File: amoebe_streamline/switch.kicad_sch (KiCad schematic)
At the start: 2 parts

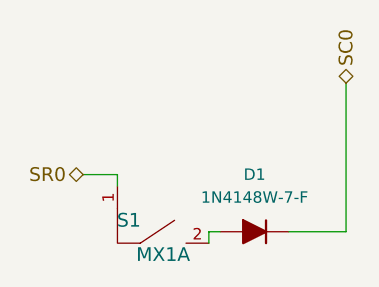
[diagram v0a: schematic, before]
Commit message: Finished schematic and routed traces
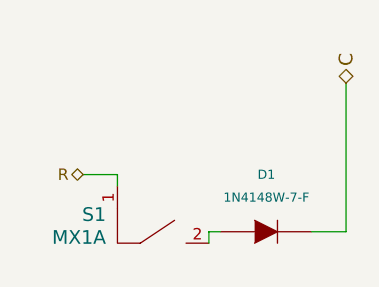
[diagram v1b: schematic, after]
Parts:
- removed D1: 1N4148W-7-F, Diode_SMD_AKL:D_SOD-123, symbol PCM_Diode_AKL:1N4148W
- removed S1: MX1A, amoeba-modules:Kailh_MX_Socket, symbol amoeba-king-rescue:MX1A-amoeba-rescue-amoeba-royale-rescue
- added D1: 1N4148W-7-F, Diode_SMD:D_SOD-123, symbol Amoebe_streamline:DIODE-amoeba-rescue
- added S1: MX1A, CustomFootprints:Kailh_socket_MX_reversible_platemount, symbol Amoebe_streamline:MX1A-amoeba-rescue
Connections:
- new net: D1.1 (A), S1.2
- new net C: D1.2 (K)
- new net R: S1.1
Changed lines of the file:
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@@
+    (stroke (width 0) (type default))
+  )
+  (wire (pts (xy 142.24 93.98) (xy 146.05 93.98))
     (stroke (width 0) (type default))
   )
   (wire (pts (xy 116.84 87.63) (xy 120.65 87.63))
-    (stroke (width 0) (type default))
-  )
-  (wire (pts (xy 139.7 93.98) (xy 146.05 93.98))
     (stroke (width 0) (type default))
   )
@@
     (stroke (width 0) (type default))
   )
-  (hierarchical_label "SC0" (shape bidirectional) (at 146.05 77.47 90) (fields_autoplaced)
+  (hierarchical_label "C" (shape bidirectional) (at 146.05 77.47 90) (fields_autoplaced)
     (effects (font (size 1.524 1.524)) (justify left))
   )
-  (hierarchical_label "SR0" (shape bidirectional) (at 116.84 87.63 180) (fields_autoplaced)
-    (effects (font (size 1.524 1.524)) (justify right))
+  (hierarchical_label "R" (shape bidirectional) (at 116.84 87.63 180) (fields_autoplaced)
+    (effects (font (size 1.27 1.27)) (justify right))
   )
-  (symbol (lib_id "amoeba-king-rescue:MX1A-amoeba-rescue-amoeba-royale-rescue") (at 125.73 99.06 0) (unit 1)
-    (in_bom yes) (on_board yes) (dnp no)
-    (property "Reference" "S1" (at 121.92 92.71 0)
-      (effects (font (size 1.524 1.524)))
+  (symbol (lib_id "Amoebe_streamline:MX1A-amoeba-rescue") (at 125.73 99.06 0) (unit 1)
+    (in_bom yes) (on_board yes) (dnp no) (fields_autoplaced)
+    (property "Reference" "S1" (at 119.38 92.075 0)
+      (effects (font (size 1.524 1.524)) (justify right))
     )
-    (property "Value" "MX1A" (at 125.73 96.52 0)
-      (effects (font (size 1.524 1.524)))
+    (property "Value" "MX1A" (at 119.38 94.615 0)
+      (effects (font (size 1.524 1.524)) (justify right))
     )
-    (property "Footprint" "amoeba-modules:Kailh_MX_Socket" (at 125.73 99.06 0)
+    (property "Footprint" "CustomFootprints:Kailh_socket_MX_reversible_platemount" (at 125.73 99.06 0)
       (effects (font (size 1.524 1.524)) hide)
     )
-    (property "Datasheet" "~" (at 125.73 99.06 0)
+    (property "Datasheet" "" (at 125.73 99.06 0)
       (effects (font (size 1.524 1.524)))
     )
@@
     (pin "2")
     (instances
-      (project "amoeba-king"
-        (path "/75875c2f-4bf0-4a86-af0a-6af4e2048374/00000000-0000-0000-0000-000055d92fdb/00000000-0000-0000-0000-000055dbae5b"
-          (reference "S1") (unit 1)
-        )
-      )
       (project "amoebe_streamline"
         (path "/f7434787-4d52-45e0-bcf8-72783deb577d/49b013cb-3077-41ab-9637-70b1ae0af3e3/3c2a59da-68dc-4b73-8d1c-aa65a6f4a5a2"
@@
     )
   )
-  (symbol (lib_id "PCM_Diode_AKL:1N4148W") (at 135.89 93.98 0) (unit 1)
+  (symbol (lib_id "Amoebe_streamline:DIODE-amoeba-rescue") (at 137.16 93.98 0) (unit 1)
     (in_bom yes) (on_board yes) (dnp no) (fields_autoplaced)
-    (property "Reference" "D1" (at 135.89 87.63 0)
-      (effects (font (size 1.27 1.27)))
+    (property "Reference" "D1" (at 137.1981 87.63 0)
+      (effects (font (size 1.016 1.016)))
     )
-    (property "Value" "1N4148W-7-F" (at 135.89 90.17 0)
-      (effects (font (size 1.27 1.27)))
+    (property "Value" "1N4148W-7-F" (at 137.1981 90.17 0)
+      (effects (font (size 1.016 1.016)))
     )
-    (property "Footprint" "Diode_SMD_AKL:D_SOD-123" (at 135.89 93.98 0)
-      (effects (font (size 1.27 1.27)) hide)
+    (property "Footprint" "Diode_SMD:D_SOD-123" (at 137.16 93.98 0)
+      (effects (font (size 1.524 1.524)) hide)
     )
-    (property "Datasheet" "https://datasheet.octopart.com/1N4148W-HE3-18-Vishay-datasheet-17291302.pdf" (at 135.89 93.98 0)
-      (effects (font (size 1.27 1.27)) hide)
+    (property "Datasheet" "" (at 137.16 93.98 0)
+      (effects (font (size 1.524 1.524)))
     )
     (pin "1")

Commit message: Fixes data lines for LED
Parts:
- S1: footprint CustomFootprints:Kailh_socket_MX_reversible_platemount -> CustomFootprints:SW_MX_reversible
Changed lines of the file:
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@@
       (effects (font (size 1.524 1.524)) (justify right))
     )
-    (property "Footprint" "CustomFootprints:Kailh_socket_MX_reversible_platemount" (at 125.73 99.06 0)
+    (property "Footprint" "CustomFootprints:SW_MX_reversible" (at 125.73 99.06 0)
       (effects (font (size 1.524 1.524)) hide)
     )
